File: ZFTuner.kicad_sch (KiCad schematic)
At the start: 4 parts, among them J101 RF_In, J102 RF_Out, J103 Tuner, J104 CAN

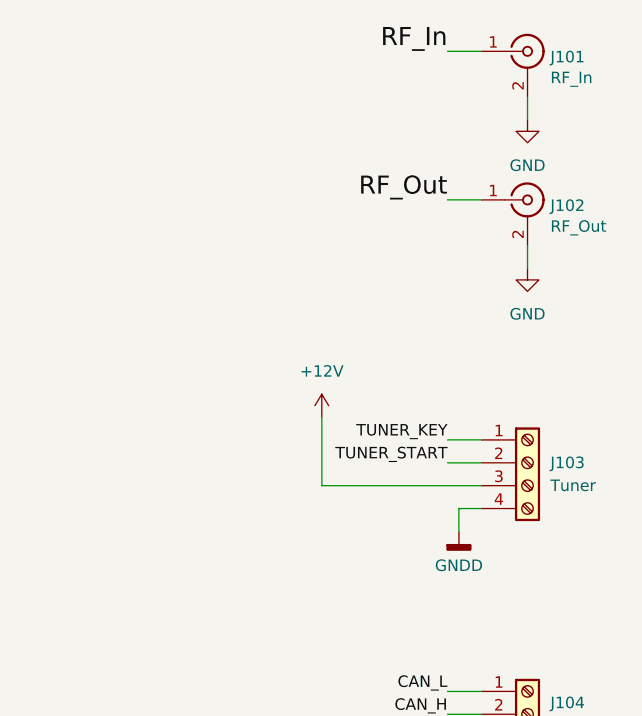
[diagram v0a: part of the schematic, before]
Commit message: Many more vias, improved some routing
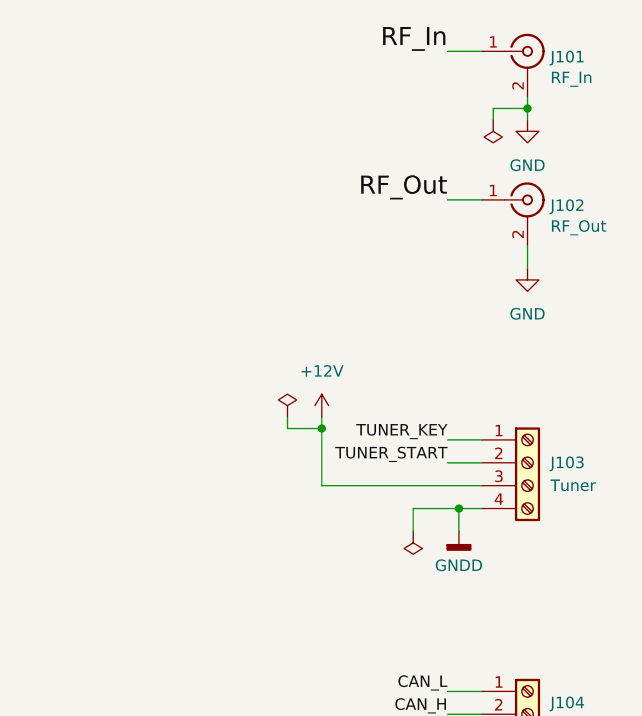
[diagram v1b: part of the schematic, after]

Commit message: Some schematic cleanup and minor fixes
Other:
- sheet Controller ports: added {S[1..4] R[1..4]}; removed Relays{S[1..4] R[1..4]}

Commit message: Replaced SMA footprints with correct connectors
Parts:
- J101, J102: footprint Connector_Coaxial:SMA_Amphenol_132289_EdgeMount -> Connector_Coaxial:SMA_Bat_Wireless_BWSMA-KE-P001_EdgeMount_1.6mm-PCB
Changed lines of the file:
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@@
 			)
 		)
-		(property "Footprint" "Connector_Coaxial:SMA_Amphenol_132289_EdgeMount"
+		(property "Footprint" "Connector_Coaxial:SMA_Bat_Wireless_BWSMA-KE-P001_EdgeMount_1.6mm-PCB"
 			(at 264.16 25.4 0)
 			(effects
@@
 			)
 		)
-		(property "Footprint" "Connector_Coaxial:SMA_Amphenol_132289_EdgeMount"
+		(property "Footprint" "Connector_Coaxial:SMA_Bat_Wireless_BWSMA-KE-P001_EdgeMount_1.6mm-PCB"
 			(at 264.16 41.91 0)
 			(effects

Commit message: Added transistors parts. Added reverse polarity protection, pending adding to layout
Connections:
- net +12V renamed +13.8V
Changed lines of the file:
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@@
+	)
+	(symbol
+		(lib_id "power:+12V")
+		(at 241.3 66.04 0)
+		(unit 1)
+		(exclude_from_sim no)
+		(in_bom yes)
+		(on_board yes)
+		(dnp no)
+		(fields_autoplaced yes)
+		(property "Reference" "#PWR0106"
+			(at 241.3 69.85 0)
+			(effects
+				(font
+					(size 1.27 1.27)
+				)
+				(hide yes)
+			)
+		)
+		(property "Value" "+13.8V"
+			(at 241.3 60.96 0)
+			(effects
+				(font
+					(size 1.27 1.27)
+				)
+			)
+		)
+		(property "Footprint" ""
+			(at 241.3 66.04 0)
+			(effects
+				(font
+					(size 1.27 1.27)
+				)
+				(hide yes)
+			)
+		)
+		(property "Datasheet" ""
+			(at 241.3 66.04 0)
+			(effects
+				(font
+					(size 1.27 1.27)
+				)
+				(hide yes)
+			)
+		)
+		(property "Description" "Power symbol creates a global label with name \"+12V\""
+			(at 241.3 66.04 0)
+			(effects
+				(font
+					(size 1.27 1.27)
+				)
+				(hide yes)
+			)
+		)
+		(pin "1"
+		)
+		(instances
+			(project "ZFTuner"
+				(path "/fdb95973-bff7-44bf-8fa0-11fcc1e3382d"
+					(reference "#PWR0106")
+					(unit 1)
+				)
+			)
+		)
 	)
 	(symbol
@@
 					(unit 1)
 				)
-			)
-		)
-	)
-	(symbol
-		(lib_id "power:+12V")
-		(at 241.3 66.04 0)
-		(unit 1)
-		(exclude_from_sim no)
-		(in_bom yes)
-		(on_board yes)
-		(dnp no)
-		(fields_autoplaced yes)
-		(property "Reference" "#PWR0103"
-			(at 241.3 69.85 0)
-			(effects
-				(font
-					(size 1.27 1.27)
-				)
-				(hide yes)
-			)
-		)
-		(property "Value" "+12V"
-			(at 241.3 60.96 0)
-			(effects
-				(font
-					(size 1.27 1.27)
-				)
-			)
-		)
-		(property "Footprint" ""
-			(at 241.3 66.04 0)
-			(effects
-				(font
-					(size 1.27 1.27)
-				)
-				(hide yes)
-			)
-		)
-		(property "Datasheet" ""
-			(at 241.3 66.04 0)
-			(effects
-				(font
-					(size 1.27 1.27)
-				)
-				(hide yes)
-			)
-		)
-		(property "Description" "Power symbol creates a global label with name \"+12V\""
-			(at 241.3 66.04 0)
-			(effects
-				(font
-					(size 1.27 1.27)
-				)
-				(hide yes)
-			)
-		)
-		(pin "1"
-		)
-		(instances
-			(project "ZFTuner"
-				(path "/fdb95973-bff7-44bf-8fa0-11fcc1e3382d"
-					(reference "#PWR0103")
-					(unit 1)
-				)

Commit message: Re-stiched GNDD vias. Added mounting holes.
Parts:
- added H101: Right_Up, MountingHole:MountingHole_3.2mm_M3_ISO7380_Pad, symbol Mechanical:MountingHole_Pad
- added H102: Right_Down, MountingHole:MountingHole_3.2mm_M3_ISO7380_Pad, symbol Mechanical:MountingHole_Pad
- added H103: Left_up, MountingHole:MountingHole_3.2mm_M3_ISO7380_Pad, symbol Mechanical:MountingHole_Pad
- added H104: Left_Down, MountingHole:MountingHole_3.2mm_M3_ISO7380_Pad, symbol Mechanical:MountingHole_Pad
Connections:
- net GND: now also H103.1, H104.1
- net GNDD: now also H101.1, H102.1

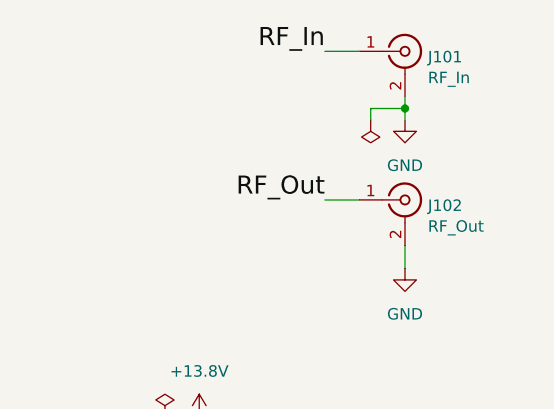
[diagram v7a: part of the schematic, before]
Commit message: A0 Production. Updated to KiCad 9.0.x
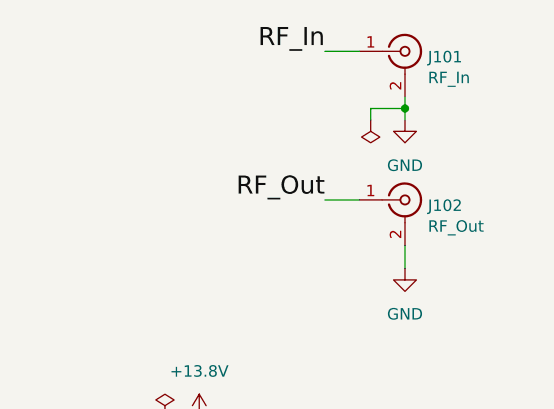
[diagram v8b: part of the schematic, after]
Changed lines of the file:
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@@
 (kicad_sch
-	(version 20231120)
+	(version 20250114)
 	(generator "eeschema")
-	(generator_version "8.0")
+	(generator_version "9.0")
 	(paper "A4")
 	(title_block
@@
 	(label "TUNER_KEY"
 		(at 255.27 68.58 180)
-		(fields_autoplaced yes)
 		(effects
 			(font
@@
 	(label "CapRels_2"
 		(at 119.38 129.54 0)
-		(fields_autoplaced yes)
 		(effects
 			(font
@@
 	(label "CAN_H"
 		(at 72.39 54.61 180)
-		(fields_autoplaced yes)
 		(effects
 			(font
@@
 	(label "RF_Out"
 		(at 170.18 109.22 0)
-		(fields_autoplaced yes)
 		(effects
 			(font
@@
 	(label "CapRels_1"
 		(at 119.38 127 0)
-		(fields_autoplaced yes)
 		(effects
 			(font
@@
 	(label "TUNER_START"
 		(at 255.27 71.12 180)
-		(fields_autoplaced yes)
 		(effects
 			(font
@@
 	(label "CAN_L"
 		(at 72.39 57.15 180)
-		(fields_autoplaced yes)
 		(effects
 			(font
@@
 	(label "TUNER_START"
 		(at 72.39 50.8 180)
-		(fields_autoplaced yes)
 		(effects
 			(font
@@
 	(label "IndRels_1"
 		(at 119.38 100.33 0)
-		(fields_autoplaced yes)
 		(effects
 			(font
@@
 	(label "RF_In"
 		(at 255.27 25.4 180)
-		(fields_autoplaced yes)
 		(effects
 			(font
@@
 	(label "RF_Out"
 		(at 170.18 135.89 0)
-		(fields_autoplaced yes)
 		(effects
 			(font
@@
 	(label "TUNER_KEY"
 		(at 72.39 48.26 180)
-		(fields_autoplaced yes)
 		(effects
 			(font
@@
 	(label "RF_Out"
 		(at 255.27 41.91 180)
-		(fields_autoplaced yes)
 		(effects
 			(font
@@
 	(label "CAN_L"
 		(at 255.27 96.52 180)
-		(fields_autoplaced yes)
 		(effects
 			(font
@@
 	(label "CAN_H"
 		(at 255.27 99.06 180)
-		(fields_autoplaced yes)
 		(effects
 			(font
@@
 	(label "RF_In"
 		(at 137.16 72.39 180)
-		(fields_autoplaced yes)
 		(effects
 			(font
@@
 	(label "IndRels_2"
 		(at 119.38 102.87 0)
-		(fields_autoplaced yes)
 		(effects
 			(font
@@
 		(at 139.7 62.23)
 		(size 17.78 12.7)
+		(exclude_from_sim no)
+		(in_bom yes)
+		(on_board yes)
+		(dnp no)
 		(stroke
 			(width 0.1524)
@@
 		(at 20.574 174.498)
 		(size 15.24 13.462)
+		(exclude_from_sim no)
+		(in_bom yes)
+		(on_board yes)
+		(dnp no)
 		(stroke
 			(width 0.1524)
@@
 		(at 139.7 93.98)
 		(size 27.94 17.78)
+		(exclude_from_sim no)
+		(in_bom yes)
+		(on_board yes)
+		(dnp no)
 		(stroke
 			(width 0.1524)
@@
 		(at 76.2 44.958)
 		(size 38.1 31.75)
+		(exclude_from_sim no)
+		(in_bom yes)
+		(on_board yes)
+		(dnp no)
 		(stroke
 			(width 0.1524)
@@
 		(at 139.7 120.65)
 		(size 27.94 17.78)
+		(exclude_from_sim no)
+		(in_bom yes)
+		(on_board yes)
+		(dnp no)
 		(stroke
 			(width 0.1524)
@@
 		)
 	)
+	(embedded_fonts no)
 )
